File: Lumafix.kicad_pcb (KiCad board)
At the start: 2 copper layers, 33.7 x 53.3 mm, 9 parts, among them U1 74LS14, U2 VICII_OUT, U3 VICII_IN

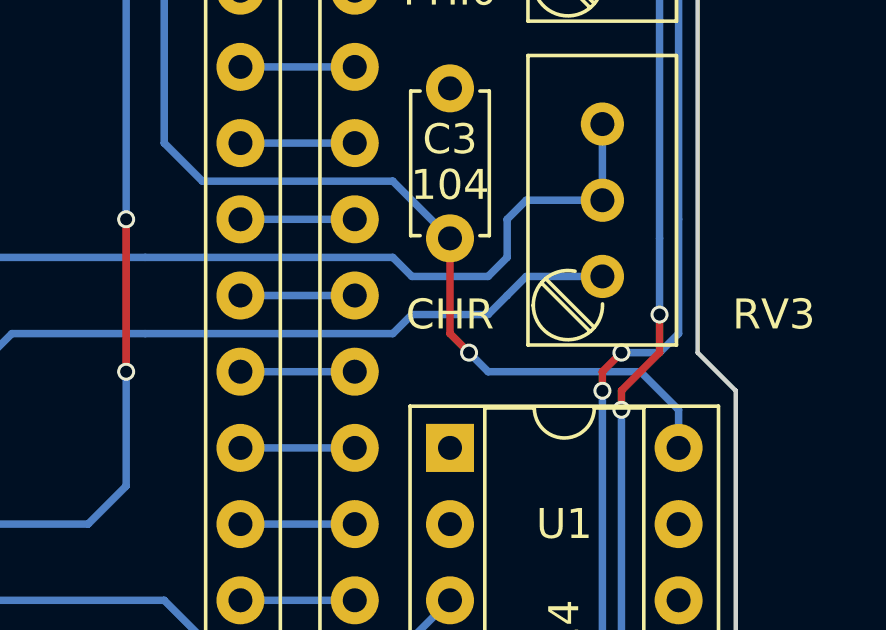
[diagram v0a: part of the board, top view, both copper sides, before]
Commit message: Misspelled CLR on PCB, oops!
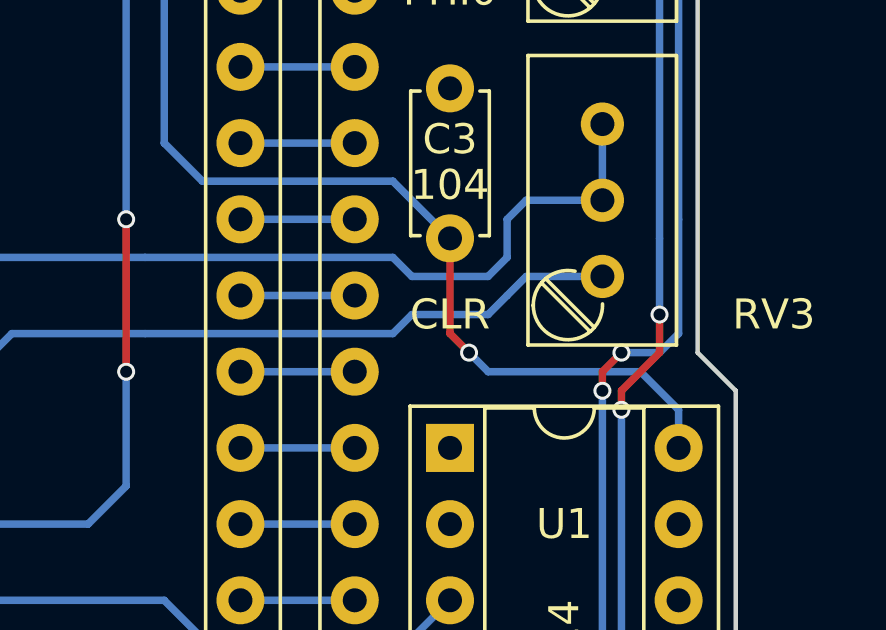
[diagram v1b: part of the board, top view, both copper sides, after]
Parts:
- RV3: value CHR -> CLR
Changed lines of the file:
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@@
     (links 60)
     (no_connects 0)
-    (area 114.224999 102.159999 150.829762 155.650001)
+    (area 114.224999 102.159999 148.030001 155.650001)
     (thickness 1.6)
     (drawings 11)
@@
     (pad_to_mask_clearance 0.2)
     (aux_axis_origin 0 0)
-    (visible_elements FFFFFF7F)
+    (visible_elements 7FFFFFFF)
     (pcbplotparams
       (layerselection 0x011fc_80000001)
@@
       (effects (font (size 1 1) (thickness 0.15)))
     )
-    (fp_text value CHR (at 1.27 5.08 360) (layer F.SilkS)
-      (effects (font (size 1 1) (thickness 0.15)))
-    )
+    (fp_text value CLR (at 1.27 5.08 360) (layer F.SilkS)
+      (effects (font (size 1 1) (thickness 0.15)))
+    )

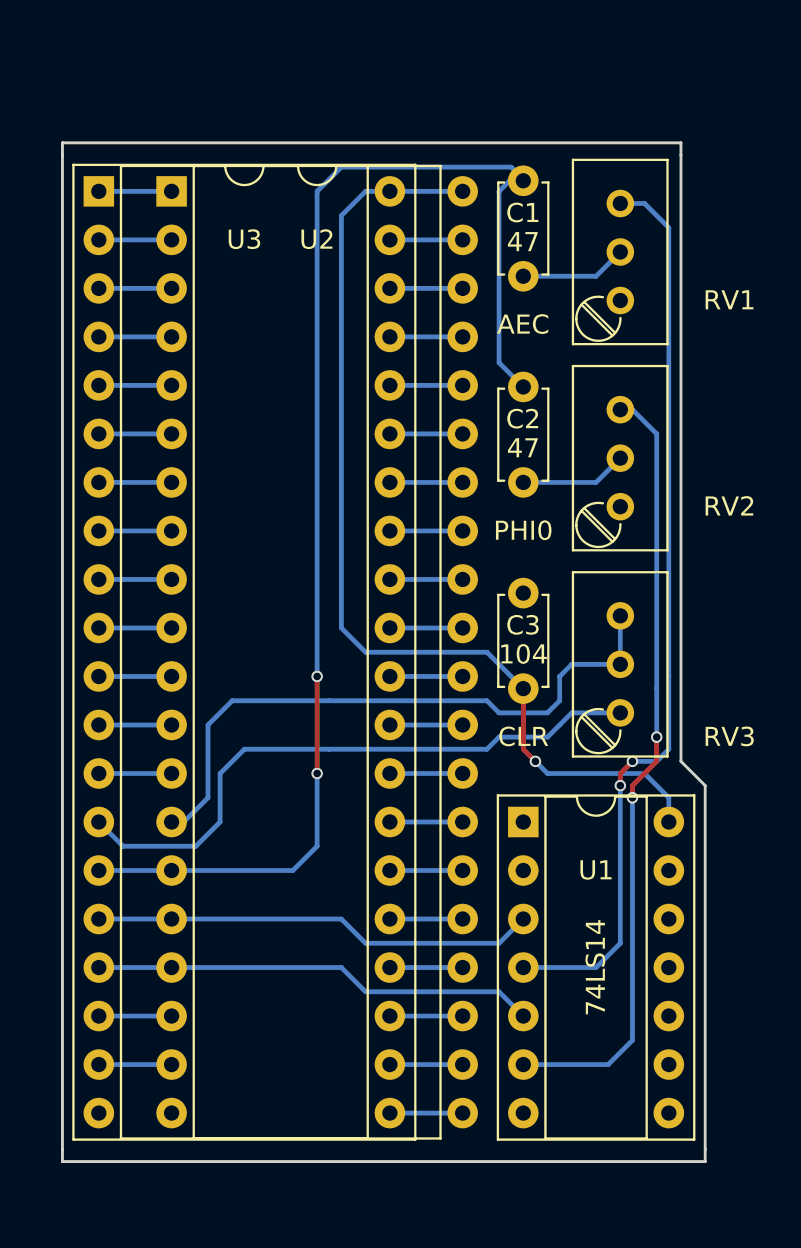
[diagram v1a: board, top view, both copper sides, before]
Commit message: Added signal bypass to module as rev. B
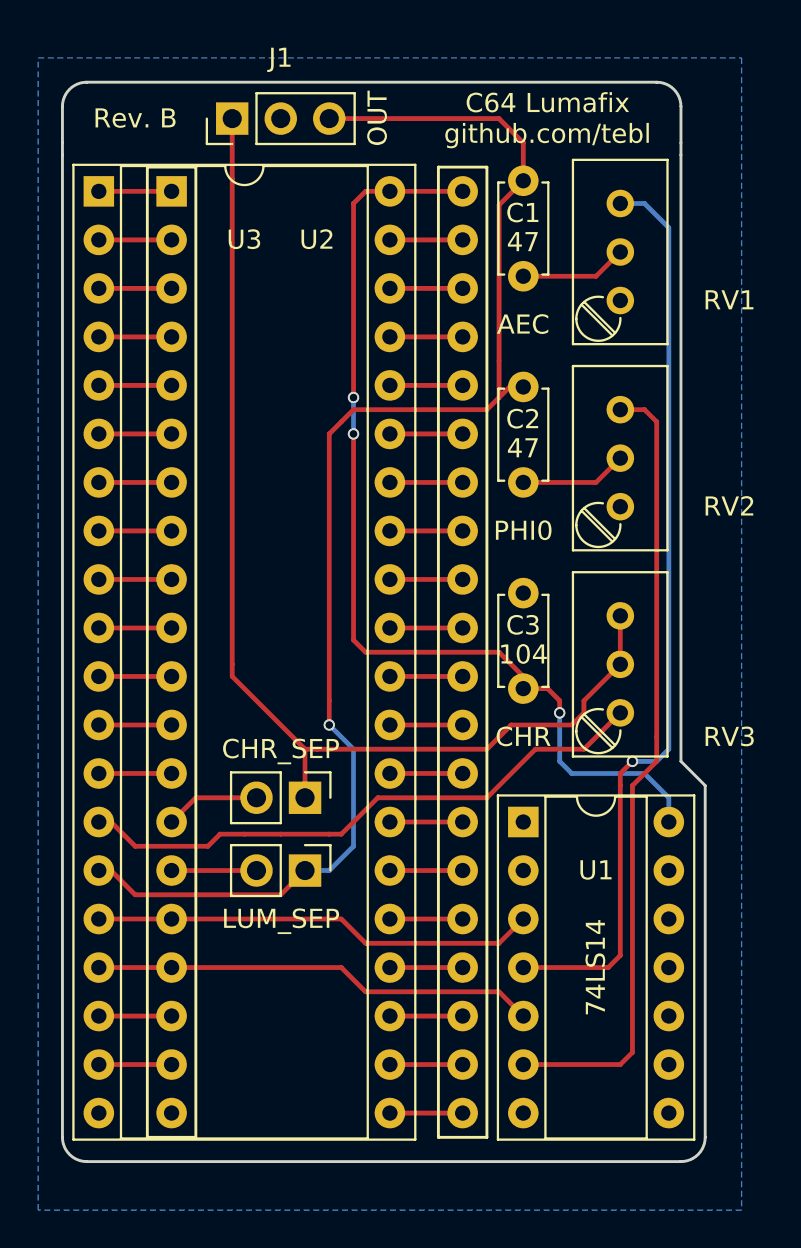
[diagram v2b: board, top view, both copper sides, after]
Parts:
- added J1: OUT, Pin_Headers:Pin_Header_Straight_1x03_Pitch2.54mm, F.Cu at (123.2, 101.0)
- added JP1: LUM_SEP, Pin_Headers:Pin_Header_Straight_1x02_Pitch2.54mm, F.Cu at (127.0, 140.3)
- added JP2: CHR_SEP, Pin_Headers:Pin_Header_Straight_1x02_Pitch2.54mm, F.Cu at (127.0, 136.5)
- RV3: value CLR -> CHR
- U2: footprint Housings_DIP:DIP-40_W15.24mm -> VICII_OUT:VICII_OUT
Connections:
- net CLR_IN renamed CHROMA_IN
- C1 pad 2: /LUM -> LUMA
- C2 pad 2: /LUM -> LUMA
- RV3 pad 2: CLR_OUT -> CHROMA
- RV3 pad 3: CLR_OUT -> CHROMA
- U2 pad 14: CLR_OUT -> CHROMA_OUT
- U2 pad 15: /LUM -> LUMA_OUT
- U3 pad 15: /LUM -> LUMA
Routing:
- net LUMA: track 0.00 -> 73.0 mm, vias 0 -> 1
- net /LUM: track 70.2 -> 0.00 mm, vias 2 -> 0
- net CHROMA: track 0.00 -> 58.4 mm
- net CLR_OUT: track 33.0 -> 0.00 mm
- net CHROMA_OUT: track 0.00 -> 4.97 mm
- net LUMA_OUT: track 0.00 -> 4.44 mm
- net CHROMA_IN: track 32.2 -> 30.7 mm
- net Net-(RV2-Pad3): track 40.9 -> 41.7 mm, vias 2 -> 0
- net Net-(RV1-Pad3): track 47.9 -> 48.3 mm, vias 2 -> 1
- net VCC: track 52.4 -> 52.3 mm, vias 1 -> 3
- added copper zone on B.Cu, net GND
- removed copper zone on F.Cu, net GND
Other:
- board size 33.7 x 53.3 mm -> 33.7 x 56.5 mm
- board text added: "C64 Lumafix github.com/tebl"
- board text added: "CHROMA"
- board text added: "CHR_SEP"
- board text added: "GND"
- board text added: "LUMA"
- board text added: "LUM_SEP"
- board text added: "Rev. B"
- board text removed: "C64 Lumafix rev. A https://hvetebolle.blogspot.com"
